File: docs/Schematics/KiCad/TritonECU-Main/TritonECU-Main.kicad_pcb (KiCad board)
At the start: 4 copper layers, 158 x 174 mm, 332 parts, among them J1 EEC-V 104, J301 VR spare, Q101 ISL9V3040S3ST, Q102 ISL9V3040S3ST, Q103 ISL9V3040S3ST, Q104 ISL9V3040S3ST, Q105 ISL9V3040S3ST, Q106 ISL9V3040S3ST, Q107 ISL9V3040S3ST, Q108 ISL9V3040S3ST, Q109 BSS138, Q201 ZXMS6005DGQTA, Q202 ZXMS6005DGQTA, Q203 ZXMS6005DGQTA, Q204 ZXMS6005DGQTA, Q205 ZXMS6005DGQTA, Q206 ZXMS6005DGQTA, Q207 ZXMS6005DGQTA, Q208 ZXMS6005DGQTA, Q401 NCV8405ASTT1G, Q402 NCV8405ASTT1G, Q403 NCV8405ASTT1G, Q404 NCV8405ASTT1G, Q405 NCV8405ASTT1G, Q406 NCV8405ASTT1G, Q407 NCV8405ASTT1G, Q408 NCV8405ASTT1G, Q501 NCV8405ASTT1G, Q502 NCV8405ASTT1G, Q503 NCV8405ASTT1G, Q504 NCV8408BDTRKG, Q505 NCV8405ASTT1G, Q506 NCV8405ASTT1G, Q507 NCV8405ASTT1G, Q701 DMN6040SVTQ-7, Q702 DMN6040SVTQ-7, U101 74HCT541, U102 TPS3823A-33DBVR, U301 MAX9926UAEE+T, U302 MAX9926UAEE+T, U303 MAX9926UAEE+T, U401 74HCT541, U402 74HC4051, U501 74HCT541, U601 TBD62083AFNG, U701 NCV8772CDT504RKG, U702 TPS2H160BQPWPRQ1, U703 LM74700QDBVRQ1, U704 LM74700QDBVRQ1, U801 ADS8588HIPM, U802 MAX6070AAUT25+T, U803 OPA2376AQDRQ1, U804 OPA2376AQDRQ1, U805 TLV9064QPWRQ1, U806 MAX6070AAUT18+T

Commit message: Carrier: Comms sheet (SCP, CAN, USB-C, microSD)
SCP: DRV8837 (coast = passive, nSLEEP 10k low), 100R per line, NUP2105L;
TLV7031 RX with the corrected 100k:100k divider to GND, MM3Z3V3 clamps,
4.7M hysteresis, 100R + SMF3.3A out. CAN: TJA1042T/3, RXD also to PA0
WKUP1, split termination 2 x 60.4R + 4.7n, NUP2105L; bus on EEC-V 42/43
(added terminals, unused cavities). USB-C device (USB4105, 5.1k CC,
USBLC6-2SC6, VBUS sense). microSD Molex 104031 on SDMMC2 1-bit, powered
through a TPS22917 on SD_PWR_EN (PG11): 3.3 V is always on.

USB-C on the right board edge; microSD parked off-board (wider than the
free strip). Scoped DRC rule for the USB4105 land pattern.

Co-Authored-By: Claude Opus 5.5 <noreply@anthropic.com>
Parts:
- added C901: 100n, Capacitor_SMD:C_0603_1608Metric_Pad1.08x0.95mm_HandSolder, F.Cu at (176.2, 176.9)
- added C902: 1u, Capacitor_SMD:C_0603_1608Metric_Pad1.08x0.95mm_HandSolder, F.Cu at (179.9, 176.9)
- added C903: 100n, Capacitor_SMD:C_0603_1608Metric_Pad1.08x0.95mm_HandSolder, F.Cu at (172.5, 178.8)
- added C904: 100n, Capacitor_SMD:C_0603_1608Metric_Pad1.08x0.95mm_HandSolder, F.Cu at (176.2, 178.8)
- added C905: 100n, Capacitor_SMD:C_0603_1608Metric_Pad1.08x0.95mm_HandSolder, F.Cu at (179.9, 178.8)
- added C906: 4.7u, Capacitor_SMD:C_0805_2012Metric_Pad1.18x1.45mm_HandSolder, F.Cu at (172.7, 180.9)
- added C907: 100n, Capacitor_SMD:C_0603_1608Metric_Pad1.08x0.95mm_HandSolder, F.Cu at (176.6, 180.6)
- added C908: 4.7n, Capacitor_SMD:C_0603_1608Metric_Pad1.08x0.95mm_HandSolder, F.Cu at (180.3, 180.6)
- added C909: 1u, Capacitor_SMD:C_0603_1608Metric_Pad1.08x0.95mm_HandSolder, F.Cu at (172.5, 183.0)
- added C910: 4.7n, Capacitor_SMD:C_0603_1608Metric_Pad1.08x0.95mm_HandSolder, F.Cu at (176.2, 183.0)
- added C911: 1u, Capacitor_SMD:C_0603_1608Metric_Pad1.08x0.95mm_HandSolder, F.Cu at (179.9, 183.0)
- added C912: 1n, Capacitor_SMD:C_0603_1608Metric_Pad1.08x0.95mm_HandSolder, F.Cu at (172.5, 184.8)
- added C913: 4.7u, Capacitor_SMD:C_0805_2012Metric_Pad1.18x1.45mm_HandSolder, F.Cu at (176.4, 185.1)
- added C914: 100n, Capacitor_SMD:C_0603_1608Metric_Pad1.08x0.95mm_HandSolder, F.Cu at (180.3, 184.8)
- added D901: NUP2105L, Package_TO_SOT_SMD:SOT-23, F.Cu at (172.8, 188.2)
- added D902: MM3Z3V3BW, Diode_SMD:D_SOD-323F, F.Cu at (176.7, 187.4)
- added D903: MM3Z3V3BW, Diode_SMD:D_SOD-323F, F.Cu at (180.3, 187.4)
- added D904: SMF3.3A, Diode_SMD:D_SMF, F.Cu at (173.2, 191.4)
- added D905: NUP2105L, Package_TO_SOT_SMD:SOT-23, F.Cu at (177.9, 192.0)
- added J901: USB4105-GF-A, Connector_USB:USB_C_Receptacle_GCT_USB4105-xx-A_16P_TopMnt_Horizontal, F.Cu at (179.3, 141.5)
- added J902: 104031-0811, Connector_Card:microSD_HC_Molex_104031-0811, F.Cu at (196.9, 36.5)
- added R901: 10k, Resistor_SMD:R_0603_1608Metric_Pad0.98x0.95mm_HandSolder, F.Cu at (177.0, 157.6)
- added R902: 100, Resistor_SMD:R_0603_1608Metric_Pad0.98x0.95mm_HandSolder, F.Cu at (180.7, 157.6)
- added R903: 100, Resistor_SMD:R_0603_1608Metric_Pad0.98x0.95mm_HandSolder, F.Cu at (172.5, 161.3)
- added R904: 100k, Resistor_SMD:R_0603_1608Metric_Pad0.98x0.95mm_HandSolder, F.Cu at (176.2, 161.3)
- added R905: 100k, Resistor_SMD:R_0603_1608Metric_Pad0.98x0.95mm_HandSolder, F.Cu at (179.9, 161.3)
- added R906: 100k, Resistor_SMD:R_0603_1608Metric_Pad0.98x0.95mm_HandSolder, F.Cu at (172.5, 163.2)
- added R907: 100k, Resistor_SMD:R_0603_1608Metric_Pad0.98x0.95mm_HandSolder, F.Cu at (176.2, 163.2)
- added R908: 4.7M, Resistor_SMD:R_0603_1608Metric_Pad0.98x0.95mm_HandSolder, F.Cu at (179.9, 163.2)
- added R909: 100, Resistor_SMD:R_0603_1608Metric_Pad0.98x0.95mm_HandSolder, F.Cu at (172.5, 165.0)
- added R910: 0, Resistor_SMD:R_0603_1608Metric_Pad0.98x0.95mm_HandSolder, F.Cu at (176.2, 165.0)
- added R911: 60.4, Resistor_SMD:R_1206_3216Metric_Pad1.30x1.75mm_HandSolder, F.Cu at (173.3, 167.3)
- added R912: 60.4, Resistor_SMD:R_1206_3216Metric_Pad1.30x1.75mm_HandSolder, F.Cu at (178.6, 167.3)
- added R913: 5.1k, Resistor_SMD:R_0603_1608Metric_Pad0.98x0.95mm_HandSolder, F.Cu at (172.5, 169.5)
- added R914: 5.1k, Resistor_SMD:R_0603_1608Metric_Pad0.98x0.95mm_HandSolder, F.Cu at (176.2, 169.5)
- added R915: 15k, Resistor_SMD:R_0603_1608Metric_Pad0.98x0.95mm_HandSolder, F.Cu at (179.9, 169.5)
- added R916: 27k, Resistor_SMD:R_0603_1608Metric_Pad0.98x0.95mm_HandSolder, F.Cu at (172.5, 171.4)
- added R917: 1M, Resistor_SMD:R_0603_1608Metric_Pad0.98x0.95mm_HandSolder, F.Cu at (176.2, 171.4)
- added R918: 100, Resistor_SMD:R_0603_1608Metric_Pad0.98x0.95mm_HandSolder, F.Cu at (179.9, 171.4)
- added R919: 100k, Resistor_SMD:R_0603_1608Metric_Pad0.98x0.95mm_HandSolder, F.Cu at (172.5, 173.2)
- added R920: 22, Resistor_SMD:R_0603_1608Metric_Pad0.98x0.95mm_HandSolder, F.Cu at (176.2, 173.2)
- added R921: 47k, Resistor_SMD:R_0603_1608Metric_Pad0.98x0.95mm_HandSolder, F.Cu at (179.9, 173.2)
- added R922: 47k, Resistor_SMD:R_0603_1608Metric_Pad0.98x0.95mm_HandSolder, F.Cu at (172.5, 175.1)
- added R923: 47k, Resistor_SMD:R_0603_1608Metric_Pad0.98x0.95mm_HandSolder, F.Cu at (176.2, 175.1)
- added R924: 47k, Resistor_SMD:R_0603_1608Metric_Pad0.98x0.95mm_HandSolder, F.Cu at (179.9, 175.1)
- added R925: 47k, Resistor_SMD:R_0603_1608Metric_Pad0.98x0.95mm_HandSolder, F.Cu at (172.5, 176.9)
- added U901: DRV8837DSGR, Package_SON:Texas_DSG0008A_WSON-8-1EP_2x2mm_P0.5mm_EP0.9x1.6mm, F.Cu at (180.1, 148.5)
- added U902: TLV7031DBVR, Package_TO_SOT_SMD:SOT-23-5, F.Cu at (172.9, 154.7)
- added U903: TJA1042T/3, Package_SO:SOIC-8_3.9x4.9mm_P1.27mm, F.Cu at (174.5, 149.9)
- added U904: USBLC6-2SC6, Package_TO_SOT_SMD:SOT-23-6, F.Cu at (177.4, 154.7)
- added U905: TPS22917DBVR, Package_TO_SOT_SMD:SOT-23-6, F.Cu at (172.9, 158.5)
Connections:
- DB3 pad D19: unconnected-(DB3-PG11-PadD19) -> SD_PWR_EN
- J1 pad 42: unconnected-(J1-Pad42) -> CAN_H
- J1 pad 43: unconnected-(J1-Pad43) -> CAN_L

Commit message: Carrier: Inputs sheet and switched rails for sleep
Inputs: one network per switch input - 4.7k pull-up to VPWR (ground-
switched only; VPWR so a TR bit closed in Park draws nothing parked),
SMF24A, 33k/15k, 10n, BAT54J to 3.3 V. TR1/2/4 and 4X4L ground-switched,
TR3A/BRAKE/ACP/TCS 12 V high-side. 4X4L mapped to EEC-V pin 14
(findings sec.14). IGN_WAKE from VPWR into PC13/WKUP4. TACH/SPEED bench
header, BOOT0 DFU solder jumper.

Switched rails: +5V and +3.3V stay up parked, so two TPS22917 load
switches on SW_RAIL_EN (PG12, 100k down) make +5V_SW / +3.3V_SW for the
running-only loads: 74HCT541 x3 and OE pull-ups, MAX9926 x3 and COUT
pull-ups, ADS8588H, OPA2376 x2, O2 bias, knock block, 74HC4051, TPS2H160B
FAULT pull-up, TFT pull-up. MCU, watchdog, CAN, SCP RX, clamps stay on.

gen_carrier_pcb.py: packer steps around existing parts, fills several
rects in turn, parks overflow below earlier parked parts.

Co-Authored-By: Claude Opus 5.5 <noreply@anthropic.com>
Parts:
- added C003: 1u, Capacitor_SMD:C_0805_2012Metric_Pad1.18x1.45mm_HandSolder, F.Cu at (85.6, 129.8)
- added C004: 1n, Capacitor_SMD:C_0603_1608Metric_Pad1.08x0.95mm_HandSolder, F.Cu at (89.5, 129.6)
- added C005: 10u, Capacitor_SMD:C_0805_2012Metric_Pad1.18x1.45mm_HandSolder, F.Cu at (93.5, 129.8)
- added C006: 1u, Capacitor_SMD:C_0805_2012Metric_Pad1.18x1.45mm_HandSolder, F.Cu at (97.6, 129.8)
- added C007: 1n, Capacitor_SMD:C_0603_1608Metric_Pad1.08x0.95mm_HandSolder, F.Cu at (81.7, 131.9)
- added C008: 10u, Capacitor_SMD:C_0805_2012Metric_Pad1.18x1.45mm_HandSolder, F.Cu at (85.6, 132.2)
- added C1001: 10n, Capacitor_SMD:C_0603_1608Metric_Pad1.08x0.95mm_HandSolder, F.Cu at (48.4, 161.8)
- added C1002: 10n, Capacitor_SMD:C_0603_1608Metric_Pad1.08x0.95mm_HandSolder, F.Cu at (59.7, 161.8)
- added C1003: 10n, Capacitor_SMD:C_0603_1608Metric_Pad1.08x0.95mm_HandSolder, F.Cu at (72.2, 161.8)
- added C1004: 10n, Capacitor_SMD:C_0603_1608Metric_Pad1.08x0.95mm_HandSolder, F.Cu at (42.8, 164.5)
- added C1005: 10n, Capacitor_SMD:C_0603_1608Metric_Pad1.08x0.95mm_HandSolder, F.Cu at (55.6, 164.5)
- added C1006: 10n, Capacitor_SMD:C_0603_1608Metric_Pad1.08x0.95mm_HandSolder, F.Cu at (66.6, 164.5)
- added C1007: 10n, Capacitor_SMD:C_0603_1608Metric_Pad1.08x0.95mm_HandSolder, F.Cu at (79.5, 164.5)
- added C1008: 10n, Capacitor_SMD:C_0603_1608Metric_Pad1.08x0.95mm_HandSolder, F.Cu at (50.4, 167.2)
- added C1009: 100n, Capacitor_SMD:C_0603_1608Metric_Pad1.08x0.95mm_HandSolder, F.Cu at (62.9, 167.2)
- added D1001: SMF24A, Diode_SMD:D_SMF, F.Cu at (44.0, 162.2)
- added D1002: BAT54J, Diode_SMD:D_SOD-323F, F.Cu at (56.1, 162.0)
- added D1003: SMF24A, Diode_SMD:D_SMF, F.Cu at (67.8, 162.2)
- added D1004: BAT54J, Diode_SMD:D_SOD-323F, F.Cu at (79.9, 162.0)
- added D1005: SMF24A, Diode_SMD:D_SMF, F.Cu at (51.2, 164.9)
- added D1006: BAT54J, Diode_SMD:D_SOD-323F, F.Cu at (63.0, 164.7)
- added D1007: SMF24A, Diode_SMD:D_SMF, F.Cu at (75.1, 164.9)
- added D1008: BAT54J, Diode_SMD:D_SOD-323F, F.Cu at (46.8, 167.4)
- added D1009: SMF24A, Diode_SMD:D_SMF, F.Cu at (58.5, 167.6)
- added D1010: BAT54J, Diode_SMD:D_SOD-323F, F.Cu at (72.7, 167.4)
- added D1011: SMF24A, Diode_SMD:D_SMF, F.Cu at (81.2, 167.6)
- added D1012: BAT54J, Diode_SMD:D_SOD-323F, F.Cu at (81.6, 136.5)
- added D1013: SMF24A, Diode_SMD:D_SMF, F.Cu at (90.1, 136.7)
- added D1014: BAT54J, Diode_SMD:D_SOD-323F, F.Cu at (98.5, 136.5)
- added D1015: SMF24A, Diode_SMD:D_SMF, F.Cu at (82.4, 139.4)
- added D1016: BAT54J, Diode_SMD:D_SOD-323F, F.Cu at (90.8, 139.2)
- added D1017: BAT54J, Diode_SMD:D_SOD-323F, F.Cu at (98.5, 139.2)
- added J1001: TACH/SPEED, Connector_PinHeader_2.54mm:PinHeader_1x03_P2.54mm_Vertical, F.Cu at (191.8, 47.0)
- added JP1001: BOOT0 DFU, Jumper:SolderJumper-2_P1.3mm_Open_RoundedPad1.0x1.5mm, F.Cu at (81.7, 144.5)
- added R002: 100, Resistor_SMD:R_0603_1608Metric_Pad0.98x0.95mm_HandSolder, F.Cu at (90.7, 125.8)
- added R003: 100, Resistor_SMD:R_0603_1608Metric_Pad0.98x0.95mm_HandSolder, F.Cu at (94.4, 125.8)
- added R004: 100k, Resistor_SMD:R_0603_1608Metric_Pad0.98x0.95mm_HandSolder, F.Cu at (81.7, 129.6)
- added R1001: 4.7k, Resistor_SMD:R_0805_2012Metric_Pad1.20x1.40mm_HandSolder, F.Cu at (39.4, 162.0)
- added R1002: 33k, Resistor_SMD:R_0805_2012Metric_Pad1.20x1.40mm_HandSolder, F.Cu at (52.3, 162.0)
- added R1003: 15k, Resistor_SMD:R_0603_1608Metric_Pad0.98x0.95mm_HandSolder, F.Cu at (63.4, 161.8)
- added R1004: 4.7k, Resistor_SMD:R_0805_2012Metric_Pad1.20x1.40mm_HandSolder, F.Cu at (76.1, 162.0)
- added R1005: 33k, Resistor_SMD:R_0805_2012Metric_Pad1.20x1.40mm_HandSolder, F.Cu at (46.7, 164.7)
- added R1006: 15k, Resistor_SMD:R_0603_1608Metric_Pad0.98x0.95mm_HandSolder, F.Cu at (59.3, 164.5)
- added R1007: 4.7k, Resistor_SMD:R_0805_2012Metric_Pad1.20x1.40mm_HandSolder, F.Cu at (70.5, 164.7)
- added R1008: 33k, Resistor_SMD:R_0805_2012Metric_Pad1.20x1.40mm_HandSolder, F.Cu at (43.0, 167.4)
- added R1009: 15k, Resistor_SMD:R_0603_1608Metric_Pad0.98x0.95mm_HandSolder, F.Cu at (54.1, 167.2)
- added R1010: 4.7k, Resistor_SMD:R_0805_2012Metric_Pad1.20x1.40mm_HandSolder, F.Cu at (66.8, 167.4)
- added R1011: 33k, Resistor_SMD:R_0805_2012Metric_Pad1.20x1.40mm_HandSolder, F.Cu at (76.6, 167.4)
- added R1012: 15k, Resistor_SMD:R_0603_1608Metric_Pad0.98x0.95mm_HandSolder, F.Cu at (39.2, 169.8)
- added R1013: 4.7k, Resistor_SMD:R_0805_2012Metric_Pad1.20x1.40mm_HandSolder, F.Cu at (85.5, 136.5)
- added R1014: 33k, Resistor_SMD:R_0805_2012Metric_Pad1.20x1.40mm_HandSolder, F.Cu at (94.7, 136.5)
- added R1015: 15k, Resistor_SMD:R_0603_1608Metric_Pad0.98x0.95mm_HandSolder, F.Cu at (42.9, 169.8)
- added R1016: 4.7k, Resistor_SMD:R_0805_2012Metric_Pad1.20x1.40mm_HandSolder, F.Cu at (87.0, 139.2)
- added R1017: 33k, Resistor_SMD:R_0805_2012Metric_Pad1.20x1.40mm_HandSolder, F.Cu at (94.7, 139.2)
- added R1018: 15k, Resistor_SMD:R_0603_1608Metric_Pad0.98x0.95mm_HandSolder, F.Cu at (46.6, 169.8)
- added R1019: 4.7k, Resistor_SMD:R_0805_2012Metric_Pad1.20x1.40mm_HandSolder, F.Cu at (81.9, 141.9)
- added R1020: 33k, Resistor_SMD:R_0805_2012Metric_Pad1.20x1.40mm_HandSolder, F.Cu at (86.0, 141.9)
- added R1021: 15k, Resistor_SMD:R_0603_1608Metric_Pad0.98x0.95mm_HandSolder, F.Cu at (50.3, 169.8)
- added R1022: 4.7k, Resistor_SMD:R_0805_2012Metric_Pad1.20x1.40mm_HandSolder, F.Cu at (90.1, 141.9)
- added R1023: 33k, Resistor_SMD:R_0805_2012Metric_Pad1.20x1.40mm_HandSolder, F.Cu at (94.2, 141.9)
- added R1024: 15k, Resistor_SMD:R_0603_1608Metric_Pad0.98x0.95mm_HandSolder, F.Cu at (54.0, 169.8)
- added R1025: 33k, Resistor_SMD:R_0805_2012Metric_Pad1.20x1.40mm_HandSolder, F.Cu at (98.3, 141.9)
- added R1026: 15k, Resistor_SMD:R_0603_1608Metric_Pad0.98x0.95mm_HandSolder, F.Cu at (57.6, 169.8)
- added R1027: 220, Resistor_SMD:R_0603_1608Metric_Pad0.98x0.95mm_HandSolder, F.Cu at (61.3, 169.8)
- added R1028: 220, Resistor_SMD:R_0603_1608Metric_Pad0.98x0.95mm_HandSolder, F.Cu at (65.0, 169.8)
- added U001: TPS22917DBVR, Package_TO_SOT_SMD:SOT-23-6, F.Cu at (82.1, 126.7)
- added U002: TPS22917DBVR, Package_TO_SOT_SMD:SOT-23-6, F.Cu at (86.6, 126.7)
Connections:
- C101 pad 1: +5V -> +5V_SW
- C301 pad 1: +5V -> +5V_SW
- C302 pad 1: +5V -> +5V_SW
- C303 pad 1: +5V -> +5V_SW
- C308 pad 1: +5V -> +5V_SW
- C309 pad 1: +5V -> +5V_SW
- C310 pad 1: +5V -> +5V_SW
- C315 pad 1: +5V -> +5V_SW
- C316 pad 1: +5V -> +5V_SW
- C317 pad 1: +5V -> +5V_SW
- C401 pad 1: +5V -> +5V_SW
- C402 pad 1: +3.3V -> +3.3V_SW
- C501 pad 1: +5V -> +5V_SW
- C801 pad 1: +5V -> +5V_SW
- C802 pad 1: +5V -> +5V_SW
- C803 pad 1: +5V -> +5V_SW
- C804 pad 1: +5V -> +5V_SW
- C805 pad 1: +5V -> +5V_SW
- C806 pad 1: +3.3V -> +3.3V_SW
- C815 pad 1: +5V -> +5V_SW
- C820 pad 1: +5V -> +5V_SW
- C826 pad 1: +3.3V -> +3.3V_SW
- C832 pad 1: +3.3V -> +3.3V_SW
- D802 pad 2: +5V -> +5V_SW
- D803 pad 2: +5V -> +5V_SW
- D804 pad 2: +5V -> +5V_SW
- D806 pad 2: +5V -> +5V_SW
- D808 pad 2: +3.3V -> +3.3V_SW
- D809 pad 2: +3.3V -> +3.3V_SW
- DB3 pad D20: unconnected-(DB3-PG12-PadD20) -> SW_RAIL_EN
- J1 pad 14: unconnected-(J1-4x4_Low_Range_FROM_THE_GEM-Pad14) -> 4X4L_IN
- R109 pad 1: +5V -> +5V_SW
- R110 pad 1: +5V -> +5V_SW
- R305 pad 1: +3.3V -> +3.3V_SW
- R310 pad 1: +3.3V -> +3.3V_SW
- R315 pad 1: +3.3V -> +3.3V_SW
- R320 pad 1: +3.3V -> +3.3V_SW
- R325 pad 1: +3.3V -> +3.3V_SW
- R330 pad 1: +3.3V -> +3.3V_SW
- R509 pad 1: +5V -> +5V_SW
- R704 pad 1: +3.3V -> +3.3V_SW
- R834 pad 1: +5V -> +5V_SW
- R849 pad 1: +3.3V -> +3.3V_SW
- U101 pad 20: +5V -> +5V_SW
- U301 pad 14: +5V -> +5V_SW
- U302 pad 14: +5V -> +5V_SW
- U303 pad 14: +5V -> +5V_SW
- U401 pad 20: +5V -> +5V_SW
- U402 pad 16: +3.3V -> +3.3V_SW
- U501 pad 20: +5V -> +5V_SW
- U801 pad 1: +5V -> +5V_SW
- U801 pad 23: +3.3V -> +3.3V_SW
- U801 pad 37: +5V -> +5V_SW
- U801 pad 38: +5V -> +5V_SW
- U801 pad 48: +5V -> +5V_SW
- U801 pad 6: +3.3V -> +3.3V_SW
- U801 pad 7: +3.3V -> +3.3V_SW
- U801 pad 8: +3.3V -> +3.3V_SW
- U803 pad 8: +5V -> +5V_SW
- U804 pad 8: +5V -> +5V_SW
- U805 pad 4: +3.3V -> +3.3V_SW
- U806 pad 3: +3.3V -> +3.3V_SW
- U806 pad 4: +3.3V -> +3.3V_SW

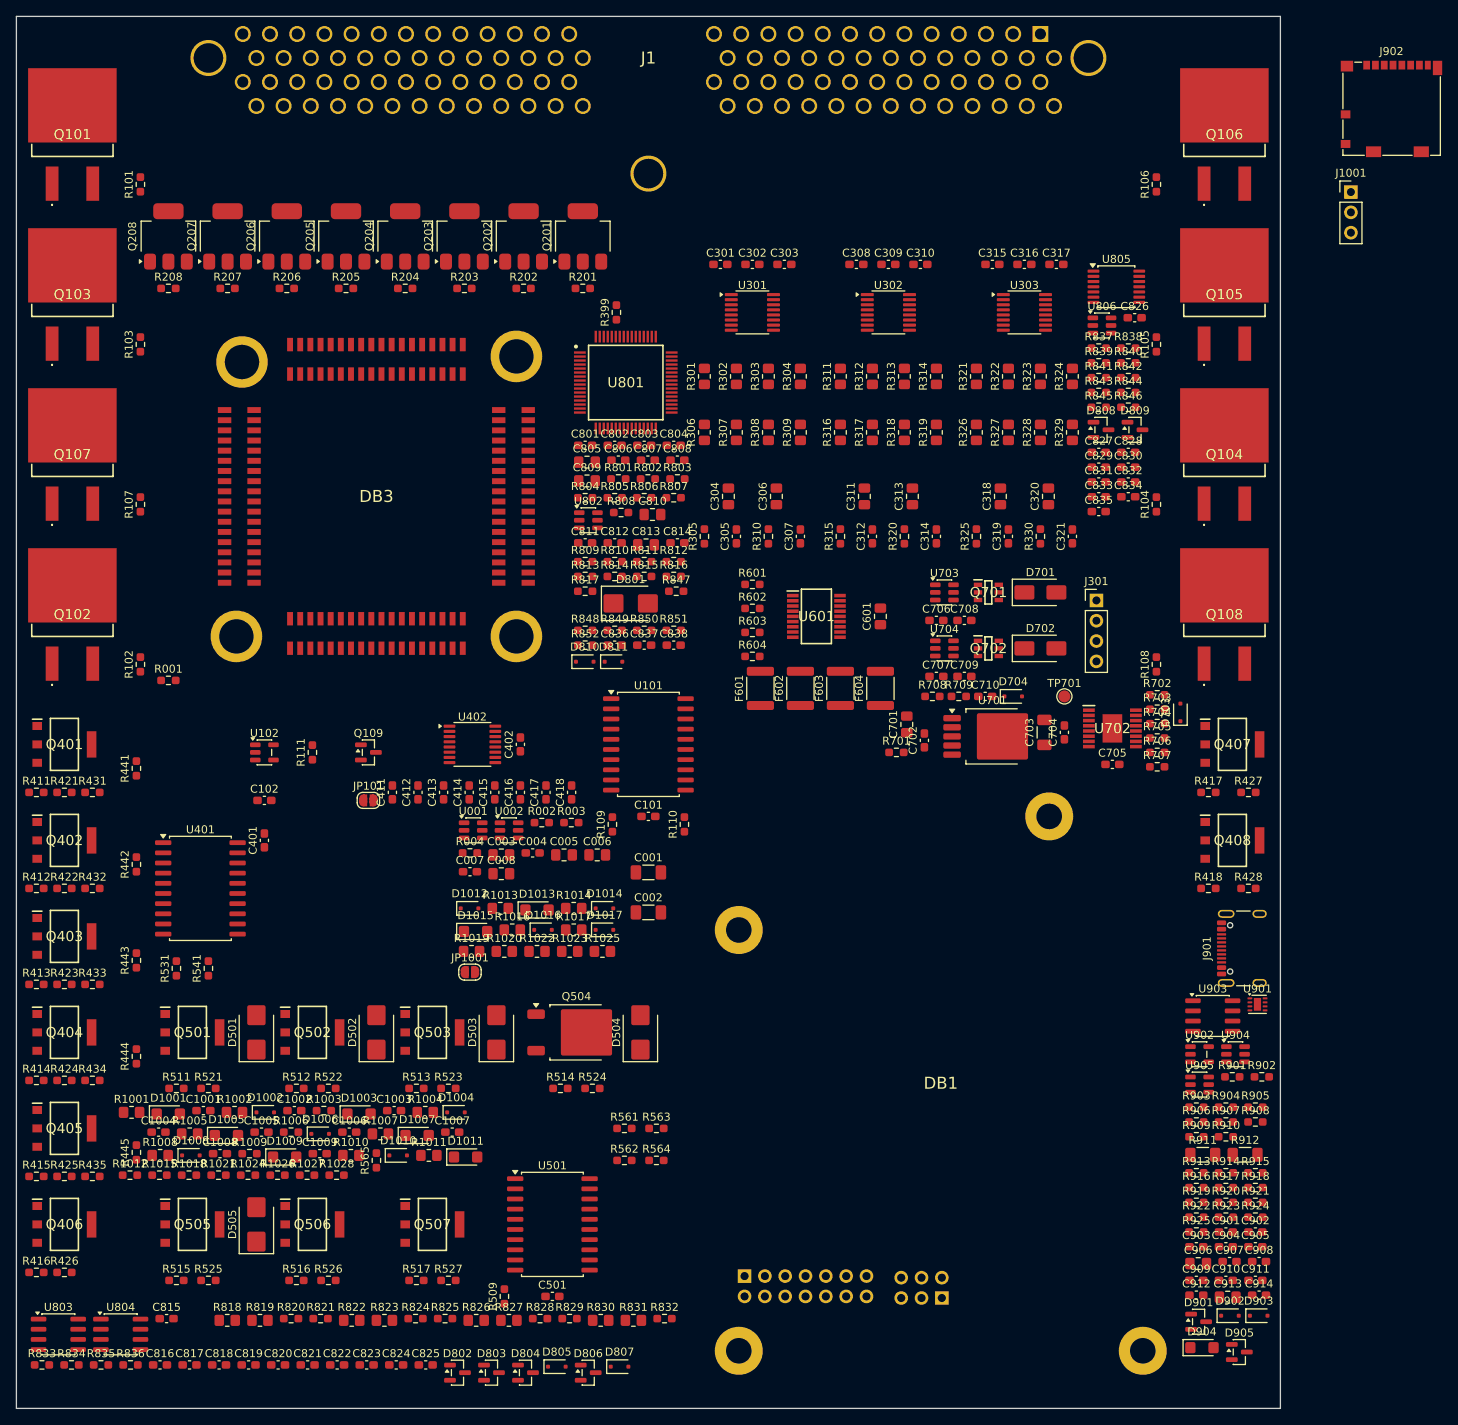
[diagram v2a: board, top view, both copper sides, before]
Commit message: Carrier PCB: place the microSD and the TACH/SPEED header
J902 microSD in the bottom-left corner, card slot to the bottom edge
(1.5 mm inboard for shield-pad edge clearance); HO2S buffers re-packed
to its right over two bands. J1001 in the gap between the EEC-V
connector and coil 6. Nothing left parked off-board.

Co-Authored-By: Claude Opus 5.5 <noreply@anthropic.com>
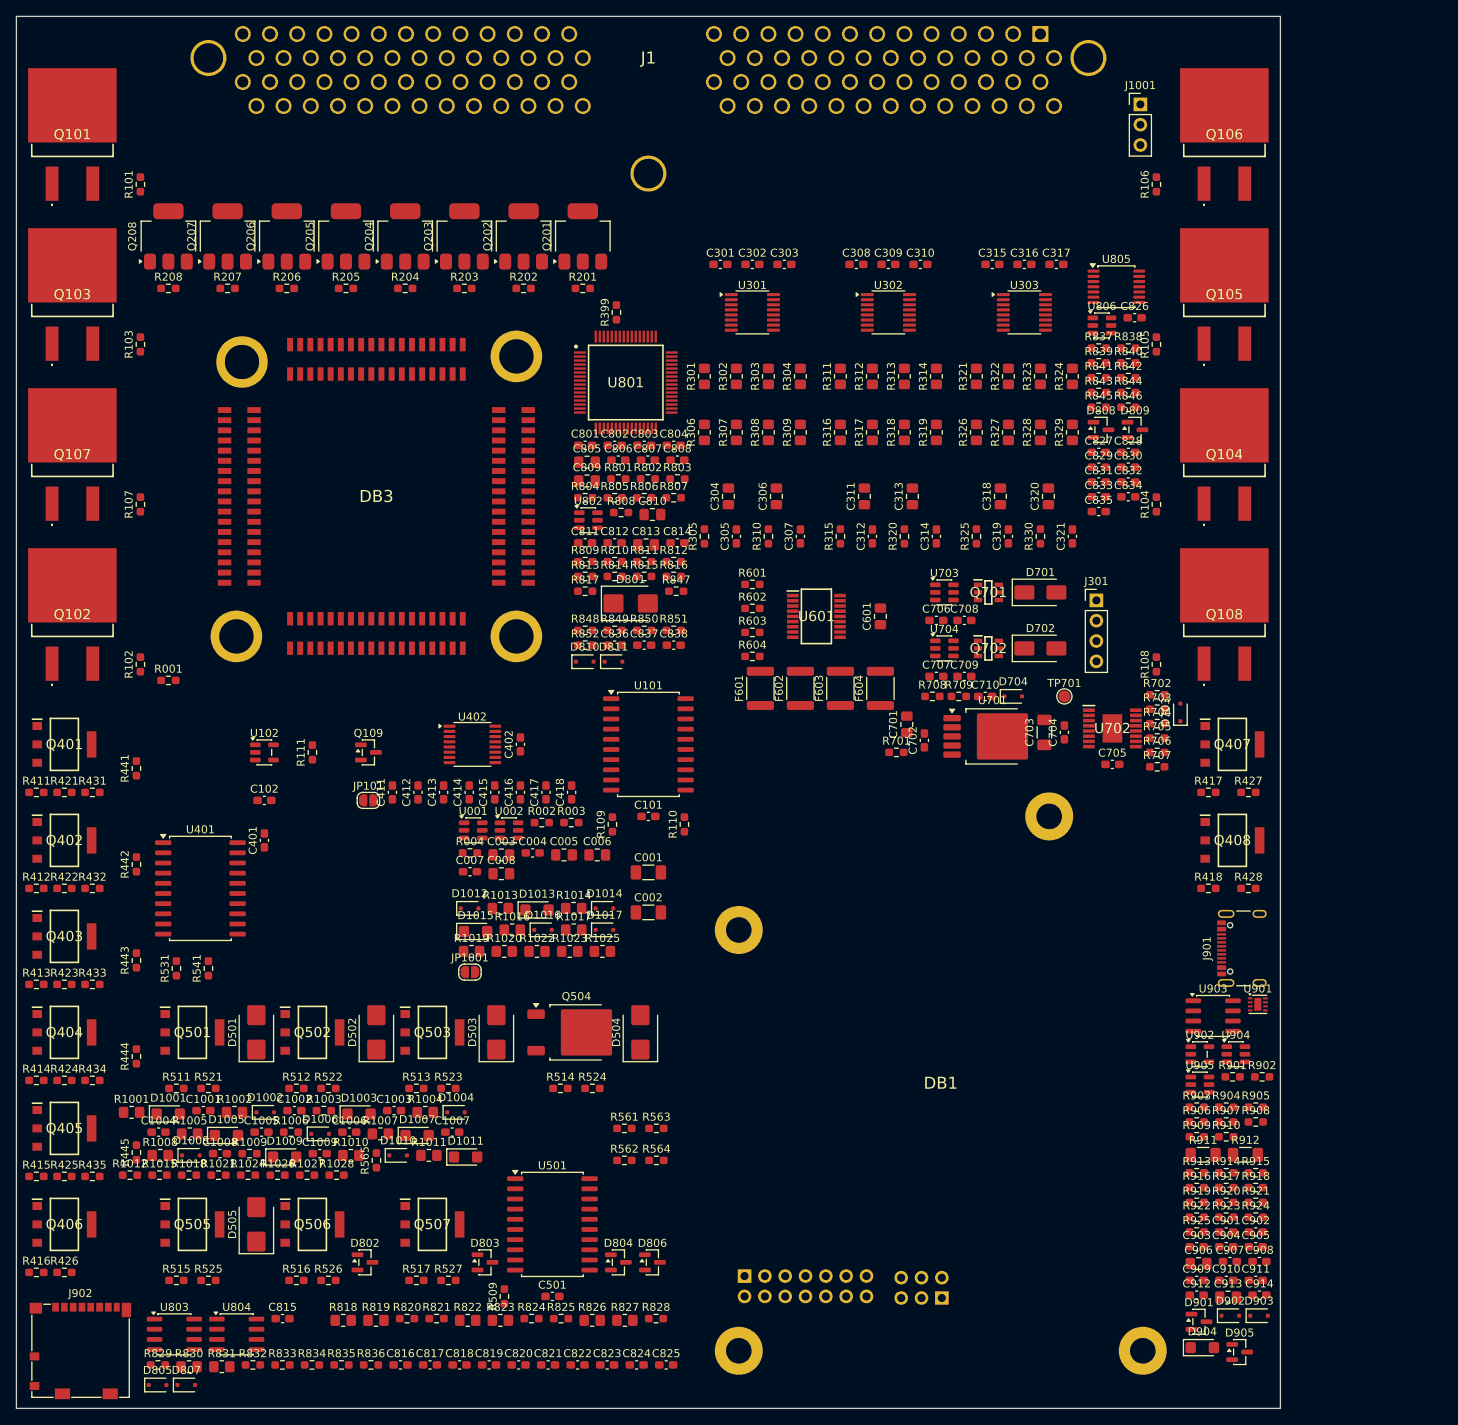
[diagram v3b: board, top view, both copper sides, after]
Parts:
- moved J902 225.7 mm to (33.0, 191.8)
- moved D807 54.2 mm to (46.2, 196.1)
- moved R831 51.8 mm to (50.7, 193.8)
- moved R832 51.8 mm to (54.6, 193.6)
- moved R829 51.8 mm to (42.7, 193.6)
- moved R830 51.8 mm to (46.6, 193.8)
- moved D805 50.0 mm to (42.6, 196.1)
- moved C821 30.1 mm to (91.5, 193.6)
- moved C817 30.1 mm to (76.7, 193.6)
- moved C822 30.1 mm to (95.2, 193.6)
- moved C823 30.1 mm to (98.8, 193.6)
- moved C824 30.1 mm to (102.5, 193.6)
- moved C825 30.1 mm to (106.2, 193.6)
- moved R833 30.1 mm to (58.3, 193.6)
- moved R834 30.1 mm to (61.9, 193.6)
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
